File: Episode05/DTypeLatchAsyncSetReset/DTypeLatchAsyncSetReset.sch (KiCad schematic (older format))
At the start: 28 parts, among them SW1 SW_Push, SW2 SW_Push, SW3 SW_Push, SW4 SW_Push, U1 74HC14, U2 74HC00, U3 74HC10

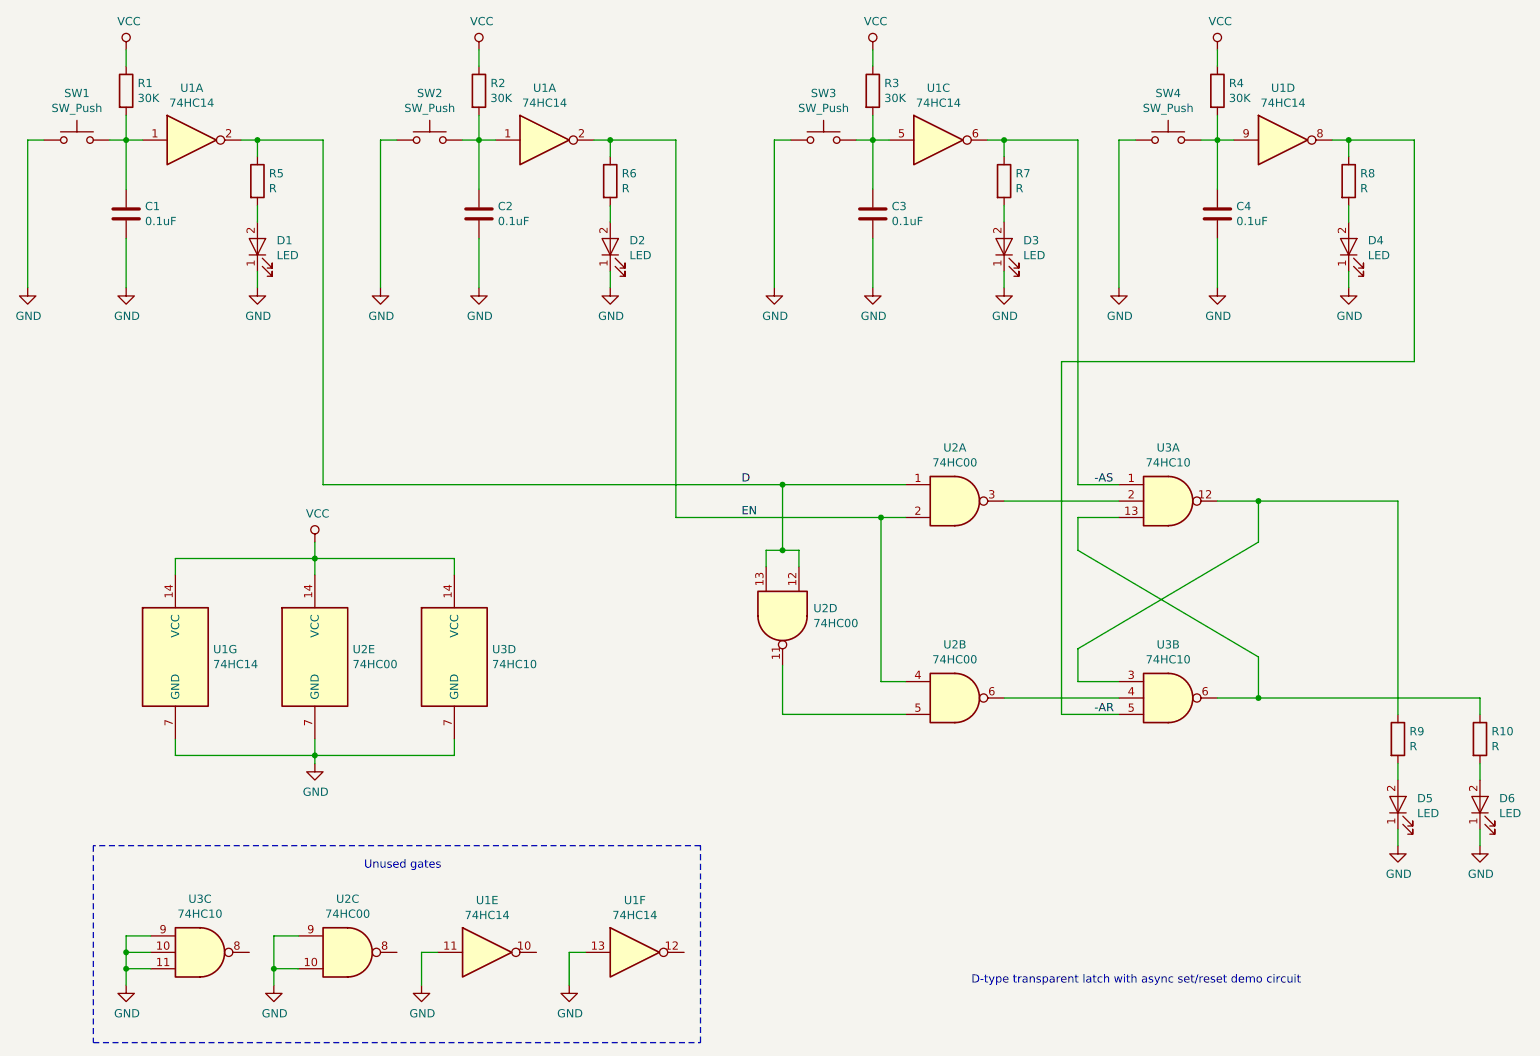
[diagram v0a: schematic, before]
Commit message: various corrections: tested working on breadboard
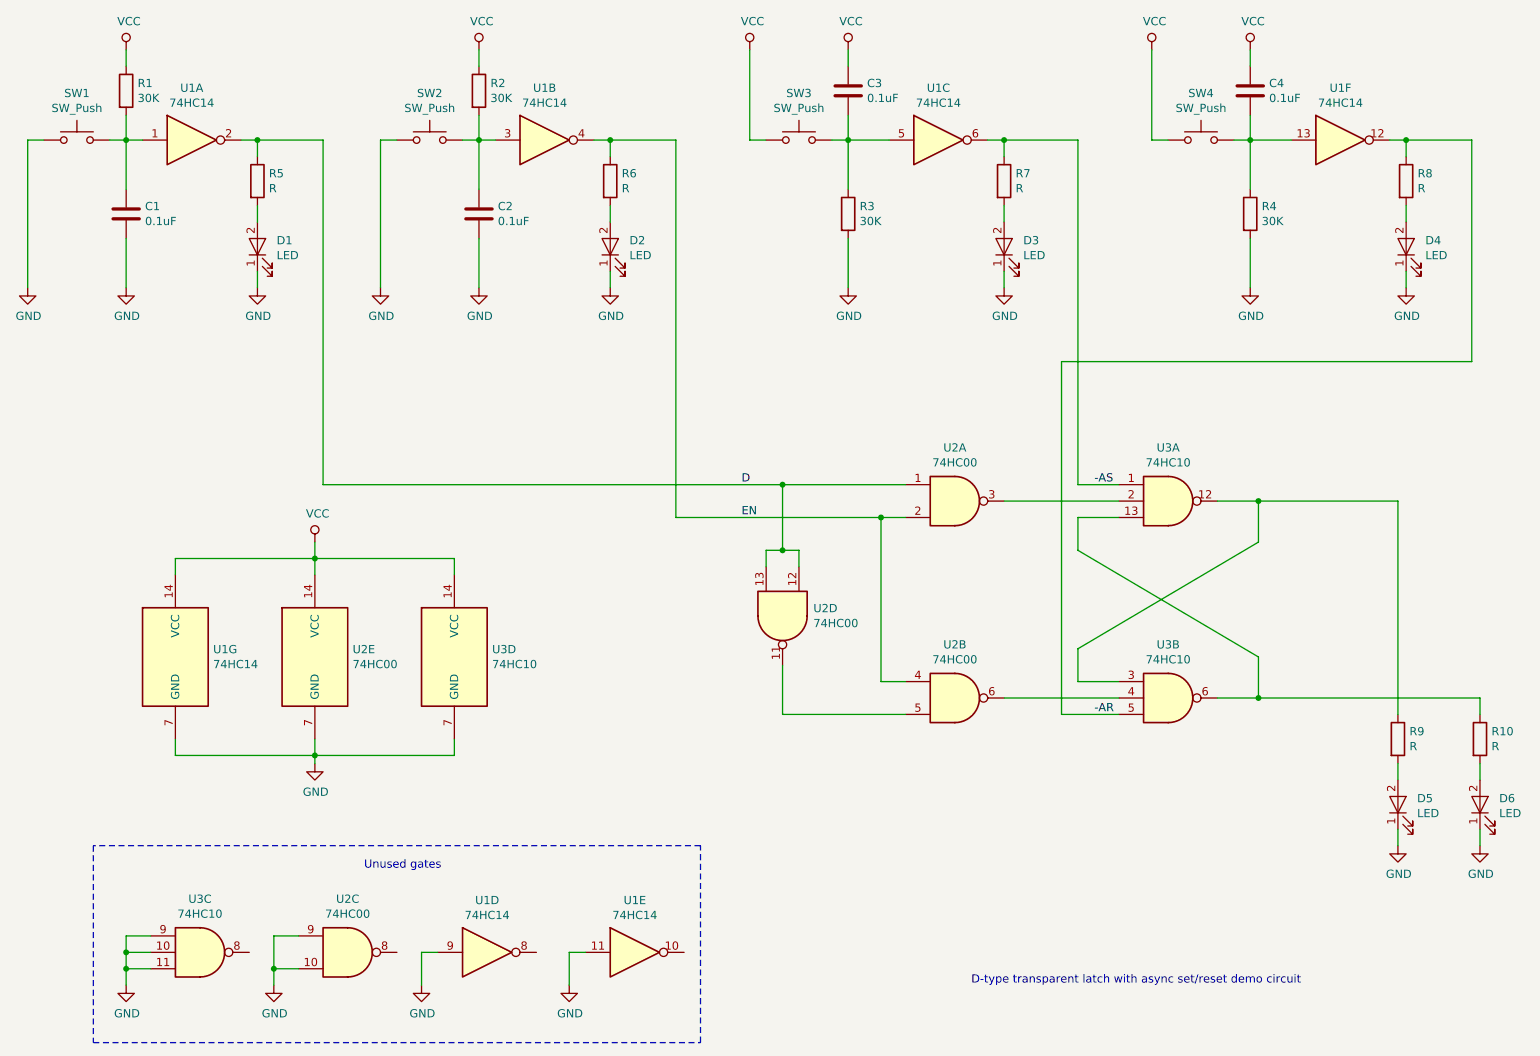
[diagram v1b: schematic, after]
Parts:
- removed U1: 74HC14, symbol 74xx:74HC14
- added unit 2 of U1
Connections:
- net -AR: now also U1.12; no longer U1.8
- net EN: now also U1.4
- net GND: now also R3.2, R4.2, U1.9; no longer C3.2, C4.2, SW3.1, SW4.1, U1.13
- net VCC: now also C3.1, C4.1, SW3.1, SW4.1; no longer R3.1, R4.1
- net at C2.1, R2.2, SW2.2: now also U1.3
- net at SW3.2, U1.5: now also C3.2, R3.1; no longer C3.1, R3.2
- new net: C4.2, R4.1, SW4.2, U1.13
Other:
- moved on the sheet: C3, C4, D4, R3, R4, R8, SW3, SW4, U1D, U1E, U1F
